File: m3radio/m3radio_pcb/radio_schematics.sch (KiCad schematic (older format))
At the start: 18 parts, among them IC201 Si4460, P201 COAX, Y201 TCXO

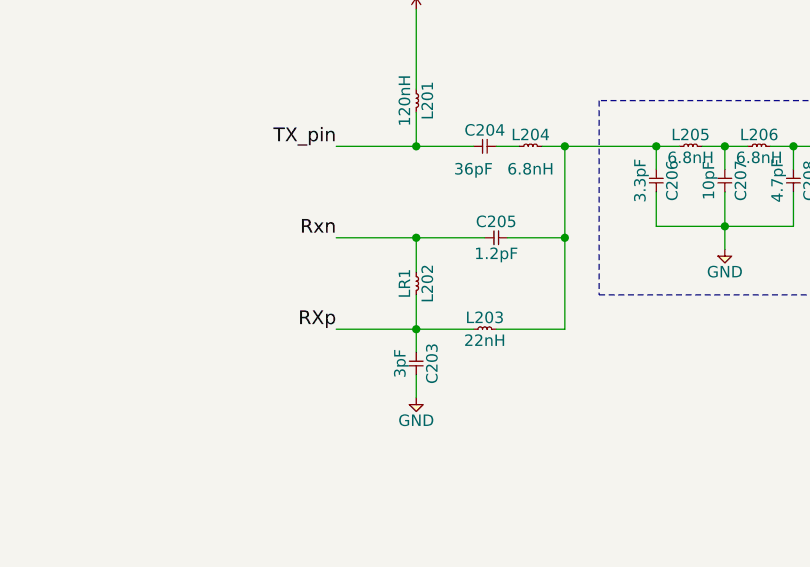
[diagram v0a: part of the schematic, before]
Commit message: Added straight up coax
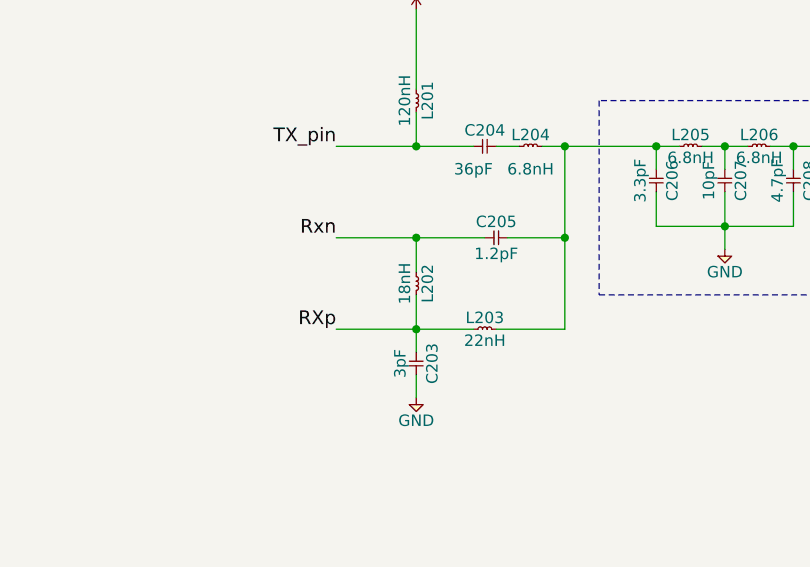
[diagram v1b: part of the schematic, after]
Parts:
- L202: value LR1 -> 18nH
- P201: footprint (none) -> M3radio:mmcxv-p-p-xx-st-th1-mkt
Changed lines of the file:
@@
 P 6250 4750
 F 0 "L202" H 6300 4800 50  0000 C CNN
-F 1 "LR1" H 6300 4700 50  0000 C CNN
+F 1 "18nH" H 6300 4700 50  0000 C CNN
 F 2 "agg:0603-L" H 6250 4750 50  0001 C CNN
 F 3 "" H 6250 4750 50  0001 C CNN
@@
 F 0 "P201" H 8500 4300 50  0000 C CNN
 F 1 "COAX" H 8500 4050 50  0000 C CNN
-F 2 "" H 8500 3990 50  0001 C CNN
+F 2 "M3radio:mmcxv-p-p-xx-st-th1-mkt" H 8500 3990 50  0001 C CNN
 F 3 "" H 8600 4100 50  0001 C CNN
 F 4 "Value" H 8500 4200 60  0001 C CNN "Fieldname"

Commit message: Make changes to schematic
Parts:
- added C4: 10nF, agg:0402, symbol C
- added C5: 100pF, agg:0402, symbol C
- added D2: ESD_DIODE, agg:0402, symbol ESD_DIODE
- C201: Digikey (none) -> Value; Farnell (none) -> 2496792; Fieldname (none) -> Value
- C202: Digikey (none) -> Value; Farnell (none) -> 2496771; Fieldname (none) -> Value
- C203: Digikey (none) -> Value; Farnell (none) -> 2210752; Fieldname (none) -> Value
- C204: Digikey (none) -> Value; Farnell (none) -> 1865427; Fieldname (none) -> Value
- C205: Digikey (none) -> Value; Farnell (none) -> 2218843; Fieldname (none) -> Value
- C206: Digikey (none) -> Value; Farnell (none) -> 2434610; Fieldname (none) -> Value
- C207: Digikey (none) -> Value; Farnell (none) -> 2496790; Fieldname (none) -> Value
- C208: Digikey (none) -> Value; Farnell (none) -> 2434644; Fieldname (none) -> Value
- C6: renamed from 1u201; value C -> 1u; Digikey (none) -> Value; Farnell (none) -> 2496814; Fieldname (none) -> Value
- L201: Digikey (none) -> Value; Farnell (none) -> 1865812; Fieldname 1865812 -> (none)
- L202: Digikey (none) -> Value; Farnell (none) -> 2424720; Fieldname (none) -> Value
- L203: Digikey (none) -> Value; Farnell (none) -> 1711755; Fieldname 1711755 -> (none)
- L204, L205, L206: Digikey (none) -> Value; Farnell (none) -> 1515395; Fieldname 1515395 -> (none)
- P201: footprint M3radio:mmcxv-p-p-xx-st-th1-mkt -> M3radio:U.FL-R-SMT-1; Digikey (none) -> Value; Farnell 1608592 -> 3908021
- Y201: footprint (none) -> M3radio:TG-5006CJ; Digikey (none) -> Value; Farnell 2405785 -> 2428493; Fieldname (none) -> Value
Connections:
- net Rxn is gone; now on net RXn: C205.1, L202.1
- net VDD is gone; now on net 3v3: L201.1
- net 3v3: now also C4.1
- net GND: now also C4.2, D2.2
- net Radio_SDN: now reaches IC201.1 (SDN)
- net Radio_GPIO1: now reaches IC201.10 (GPIO1)
- net at IC201.17 (XIN): now also C5.1; no longer Y201.3 (OUT)
- net at C208.1, L206.2, P201.1 (RF): now also D2.1
- new net: C5.2, Y201.3 (OUT)
- no-connect marks 7 -> 5
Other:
- note added: "Application note:\nSee AN627 p19 for component values\np23 (figure 6) for schematic\n\nhttps://www.silabs.com/Support%20Documents/TechnicalDocs/AN627.pdf"
- moved on the sheet: C201, C202, C6, IC201, Y201

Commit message: Make changes 25/6/16
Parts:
- Y201: footprint M3radio:TG-5006CJ -> agg:TG-5006CG; Farnell 2428493 -> 2405785
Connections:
- net 3v3: no longer C4.1, Y201.4 (VCC)
- new net 1v8: C4.1, Y201.4 (VCC)
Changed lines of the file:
@@
 Radio_nSEL
 $Comp
-L GND #PWR041
+L GND #PWR045
 U 1 1 56B22850
 P 2050 2650
-F 0 "#PWR041" H 1920 2690 50  0001 L CNN
+F 0 "#PWR045" H 1920 2690 50  0001 L CNN
 F 1 "GND" H 2050 2550 50  0000 C CNN
 F 2 "" H 2050 2650 60  0000 C CNN
@@
 $EndComp
 $Comp
-L 3v3 #PWR042
+L 3v3 #PWR046
 U 1 1 56B228AE
 P 1450 2150
-F 0 "#PWR042" H 1450 2260 50  0001 L CNN
+F 0 "#PWR046" H 1450 2260 50  0001 L CNN
 F 1 "3v3" H 1450 2240 50  0000 C CNN
 F 2 "" H 1450 2150 60  0000 C CNN
@@
 $EndComp
 $Comp
-L GND #PWR043
+L GND #PWR047
 U 1 1 56B2404E
 P 6250 5300
-F 0 "#PWR043" H 6120 5340 50  0001 L CNN
+F 0 "#PWR047" H 6120 5340 50  0001 L CNN
 F 1 "GND" H 6250 5200 50  0000 C CNN
 F 2 "" H 6250 5300 60  0000 C CNN
@@
 $EndComp
 $Comp
-L GND #PWR044
+L GND #PWR048
 U 1 1 56B24884
 P 7600 4650
-F 0 "#PWR044" H 7470 4690 50  0001 L CNN
+F 0 "#PWR048" H 7470 4690 50  0001 L CNN
 F 1 "GND" H 7600 4550 50  0000 C CNN
 F 2 "" H 7600 4650 60  0000 C CNN
@@
 $EndComp
 $Comp
-L GND #PWR045
+L GND #PWR049
 U 1 1 56B30843
 P 8350 4500
-F 0 "#PWR045" H 8220 4540 50  0001 L CNN
+F 0 "#PWR049" H 8220 4540 50  0001 L CNN
 F 1 "GND" H 8350 4400 50  0000 C CNN
 F 2 "" H 8350 4500 60  0000 C CNN
@@
 F 0 "Y201" H 1300 3000 50  0000 L CNN
 F 1 "TCXO" H 1300 2700 50  0000 L CNN
-F 2 "M3radio:TG-5006CJ" H 1300 2900 50  0001 C CNN
-F 3 "http://www.farnell.com/datasheets/1804154.pdf" H 1300 2900 50  0001 C CNN
+F 2 "agg:TG-5006CG" H 1300 2900 50  0001 C CNN
+F 3 "http://www.farnell.com/datasheets/1804153.pdf" H 1300 2900 50  0001 C CNN
 F 4 "Value" H 1500 2900 60  0001 C CNN "Digikey"
-F 5 "2428493" H 1300 2600 50  0001 L CNN "Farnell"
+F 5 "2405785" H 1300 2600 50  0001 L CNN "Farnell"
 F 6 "Value" H 1500 2900 60  0001 C CNN "Fieldname"
 	1    1500 2900
@@
 	1100 2900 1200 2900
 Wire Wire Line
-	1150 2900 1150 2850
-Wire Wire Line
 	1100 3000 1200 3000
 Wire Wire Line
 	1150 3000 1150 3050
 $Comp
-L 3v3 #PWR046
-U 1 1 56C60CB9
-P 1150 2850
-F 0 "#PWR046" H 1150 2960 50  0001 L CNN
-F 1 "3v3" H 1150 2940 50  0000 C CNN
-F 2 "" H 1150 2850 60  0000 C CNN
-F 3 "" H 1150 2850 60  0000 C CNN
-	1    1150 2850
-	1    0    0    -1
-$EndComp
-$Comp
-L GND #PWR047
+L GND #PWR050
 U 1 1 56C60D0D
 P 1150 3050
-F 0 "#PWR047" H 1020 3090 50  0001 L CNN
+F 0 "#PWR050" H 1020 3090 50  0001 L CNN
 F 1 "GND" H 1150 2950 50  0000 C CNN
 F 2 "" H 1150 3050 60  0000 C CNN
@@
 NoConn ~ 2150 2800
 $Comp
-L 3v3 #PWR048
+L 3v3 #PWR051
 U 1 1 576AEE23
 P 6250 3550
-F 0 "#PWR048" H 6250 3660 50  0001 L CNN
+F 0 "#PWR051" H 6250 3660 50  0001 L CNN
 F 1 "3v3" H 6250 3640 50  0000 C CNN
 F 2 "" H 6250 3550 60  0000 C CNN
@@
 Wire Wire Line
 	2150 3100 2050 3100
+$Comp
+L 1v8 #PWR052
+U 1 1 576ED3BF
+P 1150 2850
+F 0 "#PWR052" H 1150 2960 50  0001 L CNN
+F 1 "1v8" H 1150 2940 50  0000 C CNN
+F 2 "" H 1150 2850 60  0000 C CNN
+F 3 "" H 1150 2850 60  0000 C CNN
+	1    1150 2850
+	1    0    0    -1
+$EndComp
+Wire Wire Line
+	1150 2900 1150 2850
 $EndSCHEMATC

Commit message: add BOM
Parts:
- C201, C202, C203, C204, C205, C206, C207, C208, C4, C5, C6, L202, P201, Y201: Digikey Value -> (none); Fieldname Value -> (none)
- L201, L203, L204, L205, L206: Digikey Value -> (none)
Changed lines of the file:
@@
 F 2 "agg:0402" H 1900 2350 50  0001 C CNN
 F 3 "" H 1900 2350 50  0001 C CNN
-F 4 "Value" H 1900 2350 60  0001 C CNN "Digikey"
 F 5 "2496814" H 1900 2350 60  0001 C CNN "Farnell"
-F 6 "Value" H 1900 2350 60  0001 C CNN "Fieldname"
 	1    1900 2350
 	0    1    1    0
@@
 F 2 "agg:0402" H 1700 2350 50  0001 C CNN
 F 3 "" H 1700 2350 50  0001 C CNN
-F 4 "Value" H 1700 2350 60  0001 C CNN "Digikey"
 F 5 "2496771" H 1700 2350 60  0001 C CNN "Farnell"
-F 6 "Value" H 1700 2350 60  0001 C CNN "Fieldname"
 	1    1700 2350
 	0    1    1    0
@@
 F 2 "agg:0402" H 1450 2350 50  0001 C CNN
 F 3 "" H 1450 2350 50  0001 C CNN
-F 4 "Value" H 1450 2350 60  0001 C CNN "Digikey"
 F 5 "2496792" H 1450 2350 60  0001 C CNN "Farnell"
-F 6 "Value" H 1450 2350 60  0001 C CNN "Fieldname"
 	1    1450 2350
 	0    1    1    0
@@
 F 2 "agg:0603-L" H 6250 3950 50  0001 C CNN
 F 3 "http://www.farnell.com/datasheets/1327494.pdf" H 6250 3950 50  0001 C CNN
-F 4 "Value" H 6250 3950 60  0001 C CNN "Digikey"
 F 5 "1865812" H 6250 3950 60  0001 C CNN "Farnell"
 	1    6250 3950
@@
 F 2 "agg:0402" H 6500 4200 50  0001 C CNN
 F 3 "" H 6500 4200 50  0001 C CNN
-F 4 "Value" H 6500 4200 60  0001 C CNN "Digikey"
 F 5 "1865427" H 6500 4200 60  0001 C CNN "Farnell"
-F 6 "Value" H 6500 4200 60  0001 C CNN "Fieldname"
 	1    6500 4200
 	1    0    0    -1
@@
 F 2 "agg:0603-L" H 6700 4200 50  0001 C CNN
 F 3 "http://www.farnell.com/datasheets/321058.pdf" H 6700 4200 50  0001 C CNN
-F 4 "Value" H 6700 4200 60  0001 C CNN "Digikey"
 F 5 "1515395" H 6700 4200 60  0001 C CNN "Farnell"
 	1    6700 4200
@@
 F 2 "agg:0402" H 6550 4600 50  0001 C CNN
 F 3 "" H 6550 4600 50  0001 C CNN
-F 4 "Value" H 6550 4600 60  0001 C CNN "Digikey"
 F 5 "2218843" H 6550 4600 60  0001 C CNN "Farnell"
-F 6 "Value" H 6550 4600 60  0001 C CNN "Fieldname"
 	1    6550 4600
 	1    0    0    -1
@@
 F 2 "agg:0603-L" H 6250 4750 50  0001 C CNN
 F 3 "" H 6250 4750 50  0001 C CNN
-F 4 "Value" H 6250 4750 60  0001 C CNN "Digikey"
 F 5 "2424720" H 6250 4750 60  0001 C CNN "Farnell"
-F 6 "Value" H 6250 4750 60  0001 C CNN "Fieldname"
 	1    6250 4750
 	0    1    1    0
@@
 F 2 "agg:0603-L" H 6500 5000 50  0001 C CNN
 F 3 "http://www.farnell.com/datasheets/360119.pdf" H 6500 5000 50  0001 C CNN
-F 4 "Value" H 6500 5000 60  0001 C CNN "Digikey"
 F 5 "1711755" H 6500 5000 60  0001 C CNN "Farnell"
 	1    6500 5000
@@
 F 2 "agg:0402" H 6250 5100 50  0001 C CNN
 F 3 "" H 6250 5100 50  0001 C CNN
-F 4 "Value" H 6250 5100 60  0001 C CNN "Digikey"
 F 5 "2210752" H 6250 5100 60  0001 C CNN "Farnell"
-F 6 "Value" H 6250 5100 60  0001 C CNN "Fieldname"
 	1    6250 5100
 	0    1    1    0
@@
 F 2 "agg:0402" H 7300 4300 50  0001 C CNN
 F 3 "" H 7300 4300 50  0001 C CNN
-F 4 "Value" H 7300 4300 60  0001 C CNN "Digikey"
 F 5 "2434610" H 7300 4300 60  0001 C CNN "Farnell"
-F 6 "Value" H 7300 4300 60  0001 C CNN "Fieldname"
 	1    7300 4300
 	0    1    1    0
@@
 F 2 "agg:0402" H 7600 4300 50  0001 C CNN
 F 3 "" H 7600 4300 50  0001 C CNN
-F 4 "Value" H 7600 4300 60  0001 C CNN "Digikey"
 F 5 "2496790" H 7600 4300 60  0001 C CNN "Farnell"
-F 6 "Value" H 7600 4300 60  0001 C CNN "Fieldname"
 	1    7600 4300
 	0    1    1    0
@@
 F 2 "agg:0402" H 7900 4300 50  0001 C CNN
 F 3 "" H 7900 4300 50  0001 C CNN
-F 4 "Value" H 7900 4300 60  0001 C CNN "Digikey"
 F 5 "2434644" H 7900 4300 60  0001 C CNN "Farnell"
-F 6 "Value" H 7900 4300 60  0001 C CNN "Fieldname"
 	1    7900 4300
 	0    1    1    0
@@
 F 2 "agg:0603-L" H 7700 4200 50  0001 C CNN
 F 3 "http://www.farnell.com/datasheets/321058.pdf" H 7700 4200 50  0001 C CNN
-F 4 "Value" H 7700 4200 60  0001 C CNN "Digikey"
 F 5 "1515395" H 7700 4200 60  0001 C CNN "Farnell"
 	1    7700 4200
@@
 F 2 "agg:0603-L" H 7400 4200 50  0001 C CNN
 F 3 "http://www.farnell.com/datasheets/321058.pdf" H 7400 4200 50  0001 C CNN
-F 4 "Value" H 7400 4200 60  0001 C CNN "Digikey"
 F 5 "1515395" H 7400 4200 60  0001 C CNN "Farnell"
 	1    7400 4200
@@
 F 2 "M3radio:U.FL-R-SMT-1" H 8500 3990 50  0001 C CNN
 F 3 "http://www.farnell.com/datasheets/1947917.pdf" H 8600 4100 50  0001 C CNN
-F 4 "Value" H 8500 4200 60  0001 C CNN "Digikey"
 F 5 "3908021" H 8500 3920 50  0001 C CNN "Farnell"
-F 6 "Value" H 8500 4200 60  0001 C CNN "Fieldname"
 	1    8500 4200
 	1    0    0    -1
@@
 F 2 "agg:TG-5006CG" H 1300 2900 50  0001 C CNN
 F 3 "http://www.farnell.com/datasheets/1804153.pdf" H 1300 2900 50  0001 C CNN
-F 4 "Value" H 1500 2900 60  0001 C CNN "Digikey"
 F 5 "2405785" H 1300 2600 50  0001 L CNN "Farnell"
-F 6 "Value" H 1500 2900 60  0001 C CNN "Fieldname"
 	1    1500 2900
 	1    0    0    -1
@@
 F 2 "agg:0402" H 1100 2900 50  0001 C CNN
 F 3 "" H 1100 2900 50  0001 C CNN
-F 4 "Value" H 1100 2900 60  0001 C CNN "Digikey"
 F 5 "1414575" H 1100 2900 60  0001 C CNN "Farnell"
-F 6 "Value" H 1100 2900 60  0001 C CNN "Fieldname"
 	1    1100 2900
 	0    1    1    0
@@
 F 2 "agg:0402" H 2100 2900 50  0001 C CNN
 F 3 "" H 2100 2900 50  0001 C CNN
-F 4 "Value" H 2100 2900 60  0001 C CNN "Digikey"
 F 5 "2496792" H 2100 2900 60  0001 C CNN "Farnell"
-F 6 "Value" H 2100 2900 60  0001 C CNN "Fieldname"
 	1    2100 2900
 	-1   0    0    1
